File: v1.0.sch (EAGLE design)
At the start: 259 parts, among them J1 DC-044-A, J2 MICROSD-9P, J3 2p-2.54, J4 2p-2.54, J5 16p-2.54, J6 16p-2.54, J7 2x3p-2.54, J8 2p-2.54, Q2 SSM3J328R,LF, Q3 6pF@32.7680kHz, Q4 BSS138W-7-F, Q5 SSM3J328R,LF, SW1 SW-200D, SW2 SW-200D, SW3 SW-200D, SW4 SW-200D, SW5 SW-200D, SW6 SW-200D, SW7 SW-200D, SW8 SW-200D, U1 MCP23017-E/SO, U10 74HC139N, U11 BZX84C30, U12 SP483ECN-L, U13 FT232RL-SSOP28, U14 FT232RL-SSOP28, U15 FT232RL-SSOP28, U16 MAX213IDBR, U2 MCP79412-I/SN, U3 LOPY, U4 MAX213IDBR, U5 FT232RL-SSOP28, U6 FT232RL-SSOP28, U7 2x14p-2.54, U8 BR24G32-3, U9 MAX213IDBR, Y2 12MHZ

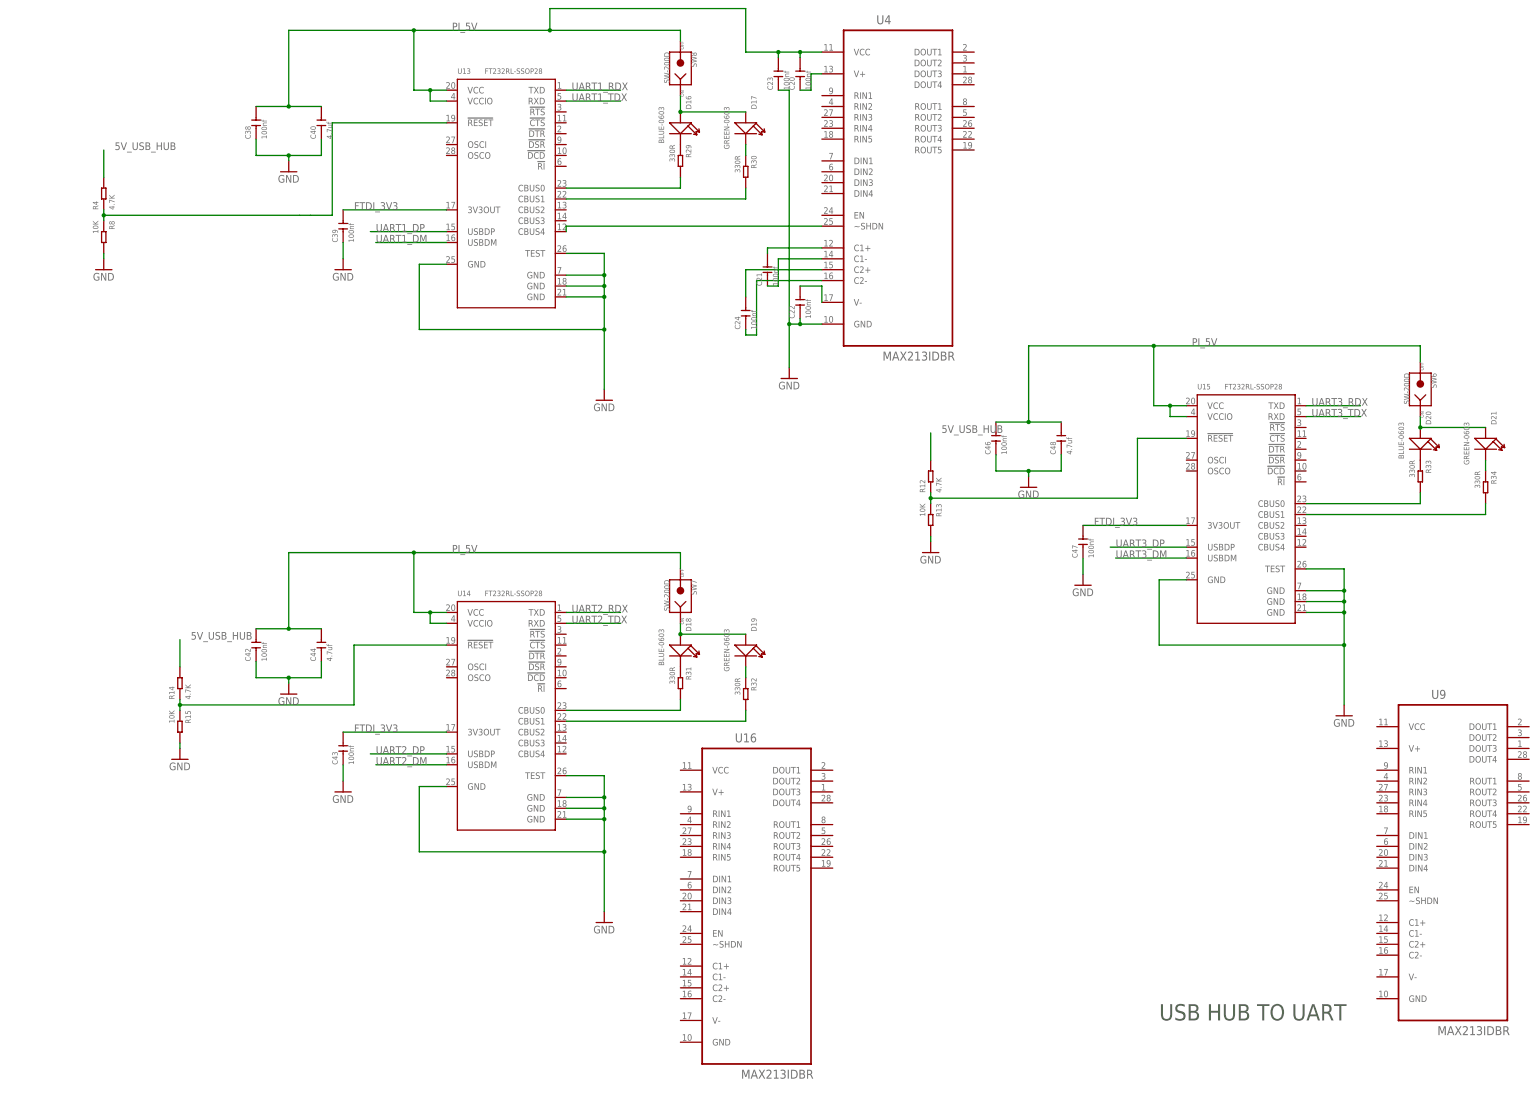
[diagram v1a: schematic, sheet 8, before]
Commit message: level converter added
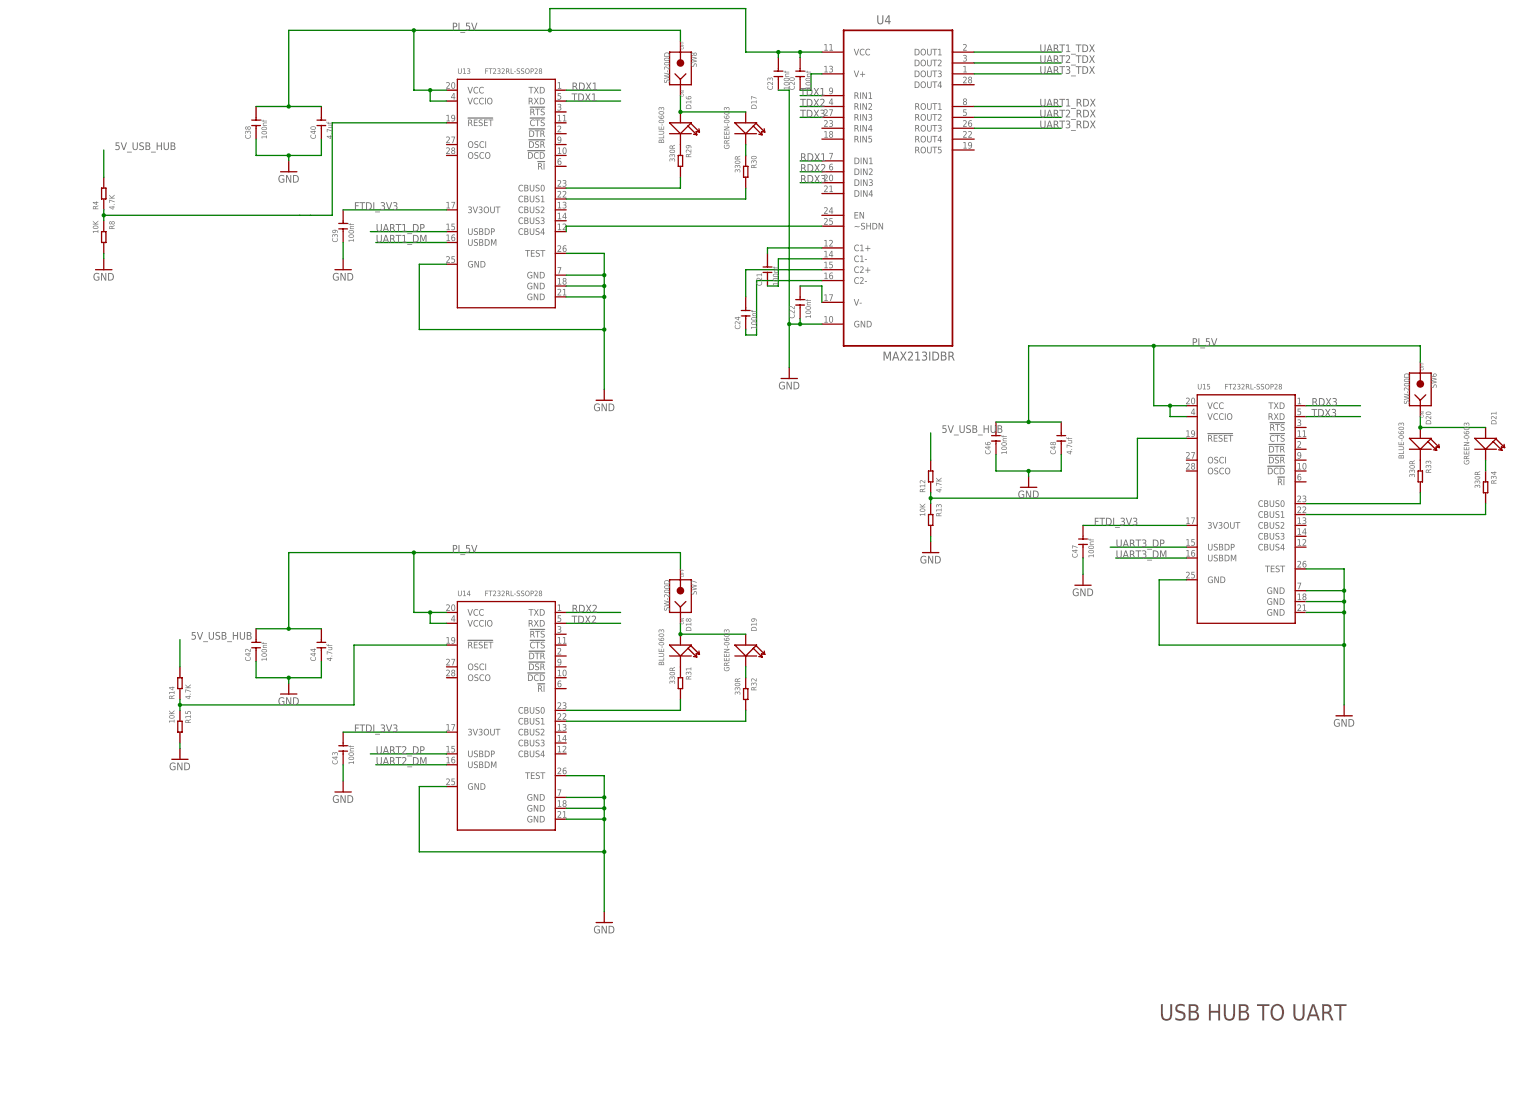
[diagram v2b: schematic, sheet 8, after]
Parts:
- removed U16, U9: MAX213IDBR, ti-max213:MAX213IDBR
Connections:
- new net RDX1: U13.TXD, U4.DIN1
- new net RDX2: U14.TXD, U4.DIN2
- new net RDX3: U15.TXD, U4.DIN3
- new net TDX1: U13.RXD, U4.RIN1
- new net TDX2: U14.RXD, U4.RIN2
- new net TDX3: U15.RXD, U4.RIN3
- net UART1_RDX: now also U4.ROUT1; no longer U13.TXD
- net UART1_TDX: now also U4.DOUT1; no longer U13.RXD
- net UART2_RDX: now also U4.ROUT2; no longer U14.TXD
- net UART2_TDX: now also U4.DOUT2; no longer U14.RXD
- net UART3_RDX: now also U4.ROUT3; no longer U15.TXD
- net UART3_TDX: now also U4.DOUT3; no longer U15.RXD
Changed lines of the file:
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@@
 <part name="R16" library="Seeed-Resistor" library_urn="urn:adsk.eagle:library:474" deviceset="SMD-RES-10K-1%-1/10W(0603)" device="" value="10K"/>
 <part name="U4" library="ti-max213" deviceset="MAX213IDBR" device=""/>
-<part name="U9" library="ti-max213" deviceset="MAX213IDBR" device=""/>
-<part name="U16" library="ti-max213" deviceset="MAX213IDBR" device=""/>
 <part name="C20" library="Seeed-Capacitor" library_urn="urn:adsk.eagle:library:464" deviceset="CERAMIC-100NF-50V-10%-X7R(0603)" device="" value="100nf"/>
 <part name="C21" library="Seeed-Capacitor" library_urn="urn:adsk.eagle:library:464" deviceset="CERAMIC-100NF-50V-10%-X7R(0603)" device="" value="100nf"/>
@@
 <instance part="SW8" gate="G$1" x="294.64" y="288.29" rot="R270"/>
 <instance part="U4" gate="A" x="345.44" y="264.16"/>
-<instance part="U9" gate="A" x="474.98" y="106.68"/>
-<instance part="U16" gate="A" x="312.42" y="96.52"/>
 <instance part="C20" gate="G$1" x="322.58" y="287.02" rot="R90"/>
 <instance part="C21" gate="G$1" x="314.96" y="241.3" rot="R90"/>
@@
 <net name="UART1_RDX" class="0">
 <segment>
-<pinref part="U13" gate="1" pin="TXD"/>
-<wire x1="267.97" y1="283.21" x2="280.67" y2="283.21" width="0.1524" layer="91"/>
-<label x="269.24" y="283.21" size="1.778" layer="95"/>
+<pinref part="U4" gate="A" pin="ROUT1"/>
+<wire x1="363.22" y1="279.4" x2="383.54" y2="279.4" width="0.1524" layer="91"/>
+<label x="378.46" y="279.4" size="1.778" layer="95"/>
 </segment>
 </net>
 <net name="UART1_TDX" class="0">
 <segment>
-<pinref part="U13" gate="1" pin="RXD"/>
-<wire x1="267.97" y1="280.67" x2="280.67" y2="280.67" width="0.1524" layer="91"/>
-<label x="269.24" y="280.67" size="1.778" layer="95"/>
+<pinref part="U4" gate="A" pin="DOUT1"/>
+<wire x1="363.22" y1="292.1" x2="383.54" y2="292.1" width="0.1524" layer="91"/>
+<label x="378.46" y="292.1" size="1.778" layer="95"/>
 </segment>
 </net>
@@
 <net name="UART2_RDX" class="0">
 <segment>
-<pinref part="U14" gate="1" pin="TXD"/>
-<wire x1="267.97" y1="161.29" x2="280.67" y2="161.29" width="0.1524" layer="91"/>
-<label x="269.24" y="161.29" size="1.778" layer="95"/>
+<pinref part="U4" gate="A" pin="ROUT2"/>
+<wire x1="363.22" y1="276.86" x2="383.54" y2="276.86" width="0.1524" layer="91"/>
+<label x="378.46" y="276.86" size="1.778" layer="95"/>
 </segment>
 </net>
 <net name="UART2_TDX" class="0">
 <segment>
-<pinref part="U14" gate="1" pin="RXD"/>
-<wire x1="267.97" y1="158.75" x2="280.67" y2="158.75" width="0.1524" layer="91"/>
-<label x="269.24" y="158.75" size="1.778" layer="95"/>
+<pinref part="U4" gate="A" pin="DOUT2"/>
+<wire x1="363.22" y1="289.56" x2="383.54" y2="289.56" width="0.1524" layer="91"/>
+<label x="378.46" y="289.56" size="1.778" layer="95"/>
 </segment>
 </net>
@@
 <net name="UART3_RDX" class="0">
 <segment>
-<pinref part="U15" gate="1" pin="TXD"/>
-<wire x1="440.69" y1="209.55" x2="453.39" y2="209.55" width="0.1524" layer="91"/>
-<label x="441.96" y="209.55" size="1.778" layer="95"/>
+<pinref part="U4" gate="A" pin="ROUT3"/>
+<wire x1="363.22" y1="274.32" x2="383.54" y2="274.32" width="0.1524" layer="91"/>
+<label x="378.46" y="274.32" size="1.778" layer="95"/>
 </segment>
 </net>
 <net name="UART3_TDX" class="0">
 <segment>
-<pinref part="U15" gate="1" pin="RXD"/>
-<wire x1="440.69" y1="207.01" x2="453.39" y2="207.01" width="0.1524" layer="91"/>
-<label x="441.96" y="207.01" size="1.778" layer="95"/>
+<pinref part="U4" gate="A" pin="DOUT3"/>
+<wire x1="363.22" y1="287.02" x2="383.54" y2="287.02" width="0.1524" layer="91"/>
+<label x="378.46" y="287.02" size="1.778" layer="95"/>
 </segment>
 </net>
@@
 </segment>
 </net>
+<net name="TDX2" class="0">
+<segment>
+<pinref part="U4" gate="A" pin="RIN2"/>
+<wire x1="327.66" y1="279.4" x2="322.58" y2="279.4" width="0.1524" layer="91"/>
+<label x="322.58" y="279.4" size="1.778" layer="95"/>
+</segment>
+<segment>
+<pinref part="U14" gate="1" pin="RXD"/>
+<wire x1="267.97" y1="158.75" x2="280.67" y2="158.75" width="0.1524" layer="91"/>
+<label x="269.24" y="158.75" size="1.778" layer="95"/>
+</segment>
+</net>
+<net name="TDX3" class="0">
+<segment>
+<pinref part="U4" gate="A" pin="RIN3"/>
+<wire x1="327.66" y1="276.86" x2="322.58" y2="276.86" width="0.1524" layer="91"/>
+<label x="322.58" y="276.86" size="1.778" layer="95"/>
+</segment>
+<segment>
+<pinref part="U15" gate="1" pin="RXD"/>
+<wire x1="440.69" y1="207.01" x2="453.39" y2="207.01" width="0.1524" layer="91"/>
+<label x="441.96" y="207.01" size="1.778" layer="95"/>
+</segment>
+</net>
+<net name="RDX1" class="0">
+<segment>
+<pinref part="U4" gate="A" pin="DIN1"/>
+<wire x1="327.66" y1="266.7" x2="322.58" y2="266.7" width="0.1524" layer="91"/>
+<label x="322.58" y="266.7" size="1.778" layer="95"/>
+</segment>
+<segment>
+<pinref part="U13" gate="1" pin="TXD"/>
+<wire x1="267.97" y1="283.21" x2="280.67" y2="283.21" width="0.1524" layer="91"/>
+<label x="269.24" y="283.21" size="1.778" layer="95"/>
+</segment>
+</net>
+<net name="RDX2" class="0">
+<segment>
+<pinref part="U4" gate="A" pin="DIN2"/>
+<wire x1="327.66" y1="264.16" x2="322.58" y2="264.16" width="0.1524" layer="91"/>
+<label x="322.58" y="264.16" size="1.778" layer="95"/>
+</segment>
+<segment>
+<pinref part="U14" gate="1" pin="TXD"/>
+<wire x1="267.97" y1="161.29" x2="280.67" y2="161.29" width="0.1524" layer="91"/>
+<label x="269.24" y="161.29" size="1.778" layer="95"/>
+</segment>
+</net>
+<net name="RDX3" class="0">
+<segment>
+<pinref part="U4" gate="A" pin="DIN3"/>
+<wire x1="327.66" y1="261.62" x2="322.58" y2="261.62" width="0.1524" layer="91"/>
+<label x="322.58" y="261.62" size="1.778" layer="95"/>
+</segment>
+<segment>
+<pinref part="U15" gate="1" pin="TXD"/>
+<wire x1="440.69" y1="209.55" x2="453.39" y2="209.55" width="0.1524" layer="91"/>
+<label x="441.96" y="209.55" size="1.778" layer="95"/>
+</segment>
+</net>
+<net name="TDX1" class="0">
+<segment>
+<pinref part="U13" gate="1" pin="RXD"/>
+<wire x1="267.97" y1="280.67" x2="280.67" y2="280.67" width="0.1524" layer="91"/>
+<label x="269.24" y="280.67" size="1.778" layer="95"/>
+</segment>
+<segment>
+<pinref part="U4" gate="A" pin="RIN1"/>
+<wire x1="327.66" y1="281.94" x2="322.58" y2="281.94" width="0.1524" layer="91"/>
+<label x="322.58" y="281.94" size="1.778" layer="95"/>
+</segment>
+</net>

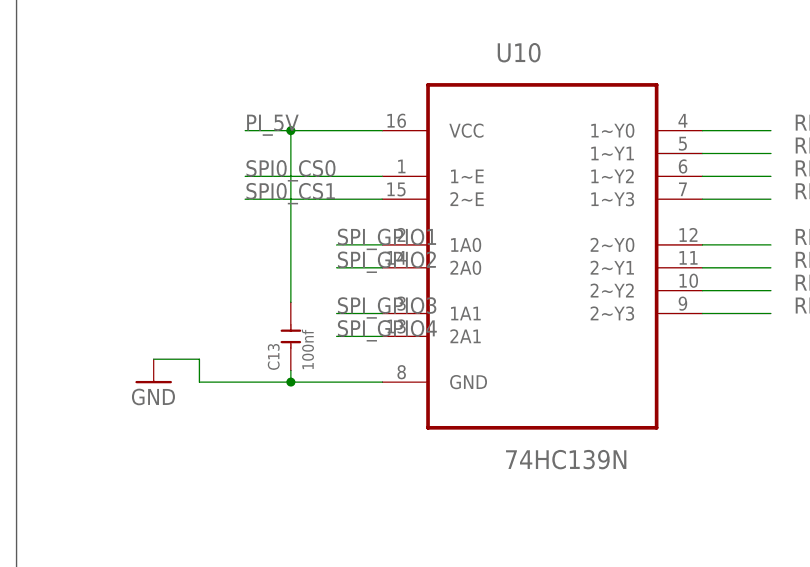
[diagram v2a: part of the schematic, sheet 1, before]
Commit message: added the mounting holes, need to tidy the board
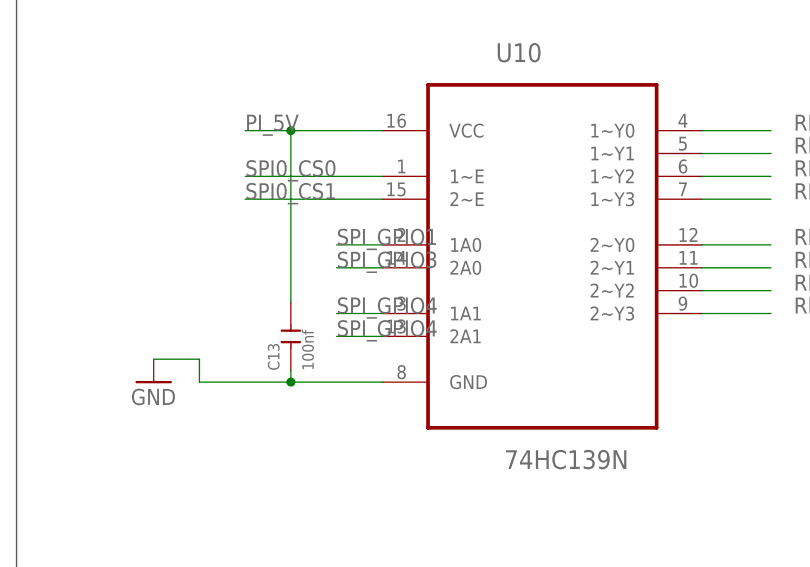
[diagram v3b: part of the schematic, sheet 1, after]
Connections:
- net SPI_GPIO2: no longer U10.2A0
- net SPI_GPIO3: now also U10.2A0; no longer U10.1A1
- net SPI_GPIO4: now also U10.1A1
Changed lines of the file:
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@@
 <net name="SPI_GPIO2" class="0">
-<segment>
-<pinref part="U10" gate="A" pin="2A0"/>
-<wire x1="200.66" y1="127" x2="195.58" y2="127" width="0.1524" layer="91"/>
-<label x="195.58" y="127" size="1.778" layer="95"/>
-</segment>
 <segment>
 <pinref part="PCB1" gate="G$1" pin="GPIO27"/>
@@
 <net name="SPI_GPIO3" class="0">
 <segment>
-<pinref part="U10" gate="A" pin="1A1"/>
-<wire x1="200.66" y1="121.92" x2="195.58" y2="121.92" width="0.1524" layer="91"/>
-<label x="195.58" y="121.92" size="1.778" layer="95"/>
-</segment>
-<segment>
 <pinref part="PCB1" gate="G$1" pin="GPIO22"/>
 <wire x1="91.44" y1="195.58" x2="74.93" y2="195.58" width="0.1524" layer="91"/>
 <label x="76.2" y="195.58" size="1.778" layer="95"/>
+</segment>
+<segment>
+<pinref part="U10" gate="A" pin="2A0"/>
+<wire x1="200.66" y1="127" x2="195.58" y2="127" width="0.1524" layer="91"/>
+<label x="195.58" y="127" size="1.778" layer="95"/>
 </segment>
 </net>
@@
 <label x="129.54" y="195.58" size="1.778" layer="95"/>
 </segment>
+<segment>
+<pinref part="U10" gate="A" pin="1A1"/>
+<wire x1="200.66" y1="121.92" x2="195.58" y2="121.92" width="0.1524" layer="91"/>
+<label x="195.58" y="121.92" size="1.778" layer="95"/>
+</segment>
 </net>

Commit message: added corrections on first 2 pages
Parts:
- added F59: SMD1206R500SF, Seeed-Fuse:SMD-PPTC-500MA(1206)
- added R17, R41: 0R, Seeed-Resistor:SMD-RES-0R-5%-1/10W(0603)
- C17: device Seeed-Capacitor-2016:CERAMIC-4.7UF-10V-10%-X5R(0603) -> Seeed-Capacitor:TANTALUM-SMD-4.7UF-16V(AVX-A)
- R36: value 1M -> 1K; device Seeed-Resistor-2016:SMD-RES-1M-1%-1/10W(0603) -> Seeed-Resistor:SMD-RES-1K-1%-1/10W(0603)
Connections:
- removed net 3V3_PROTECTED: F57.2, J7.3, J7.4
- removed net N$10: R3.2, U6.CBUS1
- new net +5V_PP: F77.2, U7.2, U7.27
- new net 3V3_P: F57.2, J7.2, J7.5
- new net FTDI1_3V3: C16.2, U6.3V3OUT
- new net GPIO12: PCB1.GPIO12, U1.INTB
- new net GPIO13: PCB1.GPIO13, U1.INTA
- new net LOPY_3V3_P: F59.2, U7.26, U7.3
- new net LOPY_3V3_PP: F56.2, U7.25, U7.4
- new net LOPY_MISO_AFTER: PCB1.GPIO6, R17.2
- new net LOPY_P2_AFTER: PCB1.GPIO5, R41.2
- net +5V: now also F77.1; no longer F76.2, U7.1, U7.24, U7.28, U7.5
- net FTDI_3V3: no longer C16.2, U6.3V3OUT
- net GND: now also C17.+, J7.3, J7.4, U7.14, U7.15; no longer C17.1, J7.2, J7.5, U7.26, U7.3
- net LOPY_3V3: now also F59.1; no longer F56.2, F77.1, F77.2, U7.2, U7.25, U7.27, U7.4
- net LOPY_MISO: now also R17.1; no longer PCB1.GPIO6
- net LOPY_P15: now also U7.24, U7.5; no longer U7.23, U7.6
- net LOPY_P16: now also U7.23, U7.6; no longer U7.22, U7.7
- net LOPY_P17: now also U7.22, U7.7; no longer U7.21, U7.8
- net LOPY_P18: now also U7.21, U7.8; no longer U7.20, U7.9
- net LOPY_P19: now also U7.20, U7.9; no longer U7.10, U7.19
- net LOPY_P2: now also R41.1; no longer PCB1.GPIO5
- net LOPY_P20: now also U7.10, U7.19; no longer U7.11, U7.18
- net LOPY_P21: now also U7.11, U7.18; no longer U7.12, U7.17
- net LOPY_P22: now also U7.12, U7.17; no longer U7.13, U7.16
- net LOPY_P23: now also U7.13, U7.16; no longer U7.14, U7.15
- net LOPY_RX1: now also LOPY_UART1-4.S; no longer LOPY_UART1-3.S
- net LOPY_TX1: now also LOPY_UART1-3.S; no longer LOPY_UART1-4.S
- net LOPY_USB_5V: now also C17.-, R1.1, R3.1; no longer C17.2, D2.+, D3.+
- net N$2: now also D3.-, U6.CBUS1; no longer U1.INTB
- net N$3: now also D2.-, U6.CBUS0; no longer U1.INTA
- net N$6: now also D3.+, R3.2; no longer D2.-, R1.1
- net N$7: now also D2.+, R1.2; no longer D3.-, R3.1
- net N$9: now also F76.2, U7.1, U7.28; no longer R1.2, U6.CBUS0
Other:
- note added: "Address: 0100000"
- moved on the sheet: F57, R1, R3
